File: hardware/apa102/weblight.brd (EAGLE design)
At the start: 31.8 x 12 mm, 16 parts, among them U1 ATtiny85-20SU

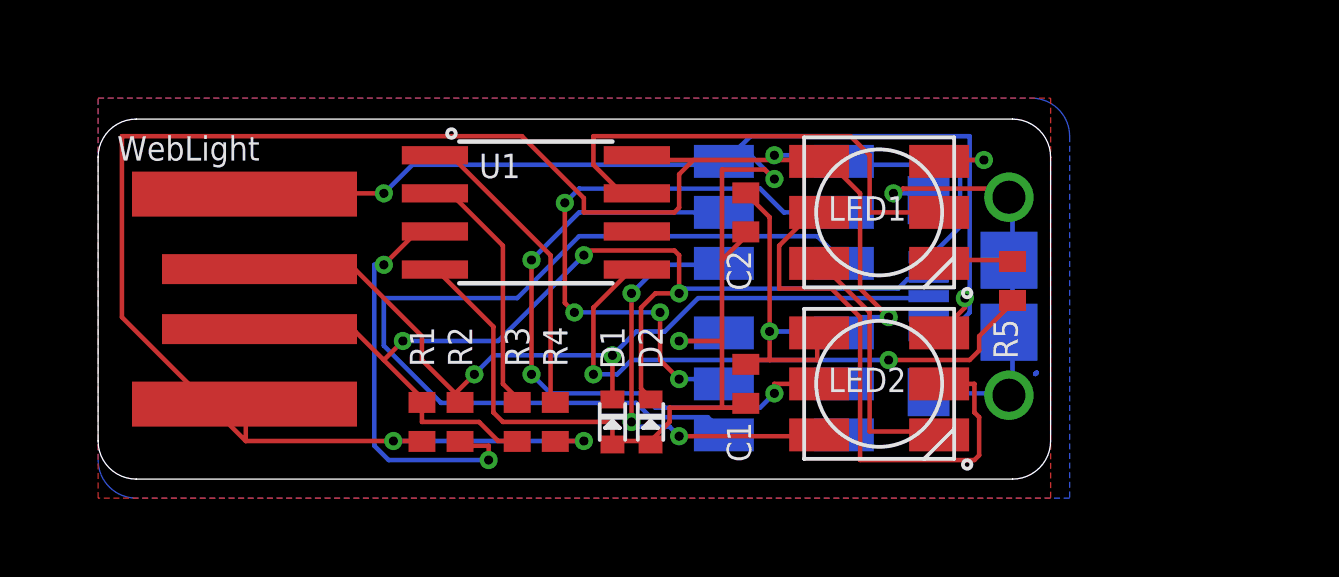
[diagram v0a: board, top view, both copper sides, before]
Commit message: Separate LED type and adopt new board versioning scheme
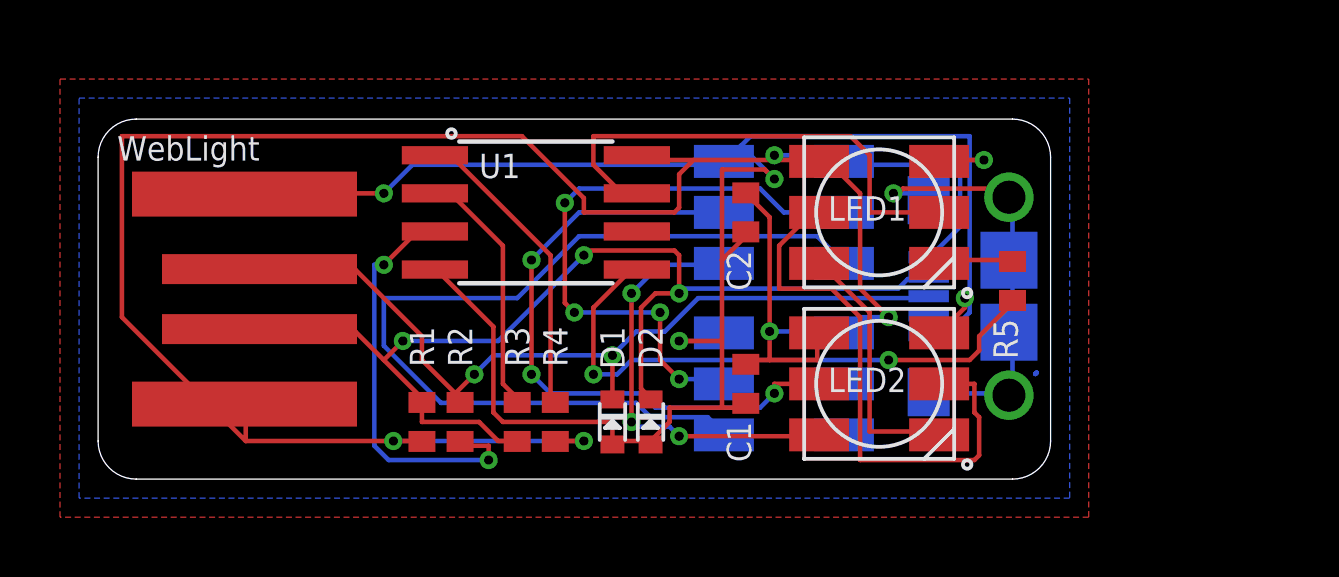
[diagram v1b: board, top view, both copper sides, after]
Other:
- board text added: "a-mf1"
- board text removed: "Version mf3"
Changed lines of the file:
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@@
 <wire x1="30.48" y1="12" x2="1.27" y2="12" width="0" layer="20"/>
 <wire x1="1.27" y1="12" x2="0" y2="10.73" width="0" layer="20" curve="90"/>
-<text x="1.27" y="0.635" size="1.016" layer="22" font="vector" rot="MR0" align="bottom-right">Version mf3</text>
+<text x="0.635" y="1.905" size="1.016" layer="22" font="vector" rot="MR0" align="bottom-right">a-mf1</text>
 <polygon width="0.4064" layer="43">
 <vertex x="0" y="12.065"/>
@@
 <vertex x="0" y="0"/>
 </polygon>
-<text x="1.27" y="2.54" size="0.8128" layer="22" font="vector" rot="MR0" align="bottom-right">sowbug.github.io/weblight</text>
+<text x="0.635" y="0.635" size="0.8128" layer="22" font="vector" rot="MR0" align="bottom-right">sowbug.github.io/weblight</text>
 <text x="0.635" y="11.43" size="0.8128" layer="21" font="vector" align="top-left">WebLight</text>
 </plain>
@@
 <via x="9.525" y="9.525" extent="1-16" drill="0.3048"/>
 <polygon width="0.4064" layer="1">
-<vertex x="0" y="12.7"/>
-<vertex x="31.75" y="12.7"/>
-<vertex x="31.75" y="-0.635"/>
-<vertex x="0" y="-0.635"/>
+<vertex x="-1.27" y="13.335"/>
+<vertex x="33.02" y="13.335"/>
+<vertex x="33.02" y="-1.27"/>
+<vertex x="-1.27" y="-1.27"/>
 </polygon>
 <polygon width="0.4064" layer="16">
-<vertex x="0" y="12.7"/>
-<vertex x="31.115" y="12.7" curve="-90"/>
-<vertex x="32.385" y="11.43"/>
+<vertex x="-0.635" y="12.7"/>
+<vertex x="32.385" y="12.7"/>
 <vertex x="32.385" y="-0.635"/>
-<vertex x="1.27" y="-0.635" curve="-90"/>
-<vertex x="0" y="0.635"/>
+<vertex x="-0.635" y="-0.635"/>
 </polygon>
 </signal>

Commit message: a-mf1
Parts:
- removed JP-USB-TOP: USBPCB, SparkFun-Connectors:USB-A-PCB
- removed R5: 470, rcl:R0402
- added HOLE1, HOLE2, HOLE3, HOLE4: MOUNTINGHOLE2.0, microbuilder:MOUNTINGHOLE_2.0_PLATED
- C1: value 10uF -> 1uF
- moved R1 16.2 mm to (26.7, 5.08), turned to 0 degrees
- moved LED4 16.1 mm to (8.13, 9.65), flipped to the top, turned to 180 degrees
- moved LED3 15.8 mm to (8.13, 3.05), flipped to the top, turned to 180 degrees
- moved R2 14.7 mm to (26.7, 3.81), turned to 180 degrees
- moved R3 12.7 mm to (26.7, 2.54), turned to 0 degrees
- moved D1 11.4 mm to (26.7, 8.26), turned to 90 degrees
- moved R4 11.4 mm to (26.7, 1.27), turned to 180 degrees
- moved LED1 11.3 mm to (14.7, 9.65), turned to 180 degrees
- moved LED2 11.3 mm to (14.7, 3.05), turned to 180 degrees
- moved D2 9.69 mm to (26.7, 6.99), turned to 90 degrees
- moved C1 9.69 mm to (26.7, 11.4), turned to 180 degrees
- moved U1 6.60 mm to (20.7, 6.35), turned to 0 degrees
- moved JP-USB-MICRO 6.36 mm to (35.3, 6.35), flipped to the top, turned to 90 degrees
- moved C2 5.24 mm to (26.7, 10.2), turned to 180 degrees
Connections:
- removed net DIN_RAW: R5.2, U1.5
- net DIN_1: now also U1.5; no longer R5.1
- net GND: now also C1.1, C2.1; no longer C1.2, C2.2, JP-USB-TOP.GND
- net USB_D_MINUS: now also R2.2; no longer R3.2
- net USB_D_MINUS_RAW: now also R1.2, R2.1; no longer JP-USB-TOP.USB_M, R1.1, R3.1
- net USB_D_PLUS: now also R3.1; no longer R2.2
- net USB_D_PLUS_RAW: now also R3.2; no longer JP-USB-TOP.USB_P, R2.1
- net VCC: now also C1.2, C2.2, R1.1; no longer C1.1, C2.1, JP-USB-TOP.5V, R1.2
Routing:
- net USB_D_MINUS_RAW: track 36.6 -> 10.6 mm, vias 3 -> 0
- net DIN_4: track 30.7 -> 8.36 mm
- net DIN_RAW: track 19.5 -> 0.00 mm, vias 2 -> 0
- net CLK_4: track 20.5 -> 8.51 mm, vias 4 -> 0
- net CLK_2: track 18.7 -> 8.60 mm
- net GND: track 68.8 -> 59.0 mm, vias 5 -> 4
- net VCC: track 84.2 -> 74.5 mm, vias 5 -> 4
- net DIN_1: track 2.56 -> 11.6 mm
- net CLK_3: track 21.4 -> 12.8 mm, vias 3 -> 0
- net USB_D_PLUS: track 14.1 -> 6.01 mm, vias 2 -> 0
- net CLK_1: track 16.5 -> 9.02 mm, vias 0 -> 2
- net USB_D_PLUS_RAW: track 28.0 -> 33.0 mm, vias 2 -> 0
- net SLD: track 15.2 -> 12.1 mm, vias 1 -> 0
- net DIN_3: track 14.2 -> 11.2 mm, vias 3 -> 2
- net N_RESET: track 10.2 -> 8.31 mm
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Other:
- board size 31.8 x 12 mm -> 38.1 x 12.7 mm
- board text removed: "sowbug.github.io/weblight"

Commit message: Forgot ICSP
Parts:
- added ICSP: POGOPIN-CONNONEHOLE, Protofusion:POGOPROG-CONN-1H
- JP-USB-MICRO: value (none) -> USB
- moved R4 5.08 mm to (21.6, 1.27)
- moved U1 1.27 mm to (20.7, 7.62)
- moved R2 1.27 mm to (26.7, 2.54), turned to 0 degrees
- moved R3 1.27 mm to (26.7, 1.27), turned to 180 degrees
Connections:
- removed net CLK_1: LED1.CI, U1.7
- removed net DIN_1: LED1.DI, U1.5
- new net CLK_1/SCK: ICSP.4, LED1.CI, U1.7
- new net DIN_1/MOSI: ICSP.2, LED1.DI, U1.5
- new net MISO: ICSP.3, U1.6
- net GND: now also ICSP.5
- net N_RESET: now also ICSP.1
- net USB_D_MINUS: now also R3.2; no longer R2.2
- net USB_D_MINUS_RAW: now also R3.1; no longer R2.1
- net USB_D_PLUS: now also R2.1; no longer R3.1
- net USB_D_PLUS_RAW: now also R2.2; no longer R3.2
- net VCC: now also ICSP.6
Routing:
- net DIN_1/MOSI: track 0.00 -> 27.4 mm, vias 0 -> 2
- net MISO: track 0.00 -> 16.8 mm, vias 0 -> 1
- net CLK_1/SCK: track 0.00 -> 15.9 mm, vias 0 -> 2
- net N_RESET: track 8.31 -> 20.3 mm, vias 0 -> 1
- net DIN_1: track 11.6 -> 0.00 mm
- net CLK_1: track 9.02 -> 0.00 mm, vias 2 -> 0
- net USB_D_MINUS_RAW: track 10.6 -> 13.8 mm
- net USB_D_PLUS_RAW: track 33.0 -> 30.1 mm, vias 0 -> 2
- net GND: track 59.0 -> 56.6 mm, vias 4 -> 3
- net VCC: track 74.5 -> 76.5 mm, vias 4 -> 3
- net DIN_3: track 11.2 -> 10.7 mm

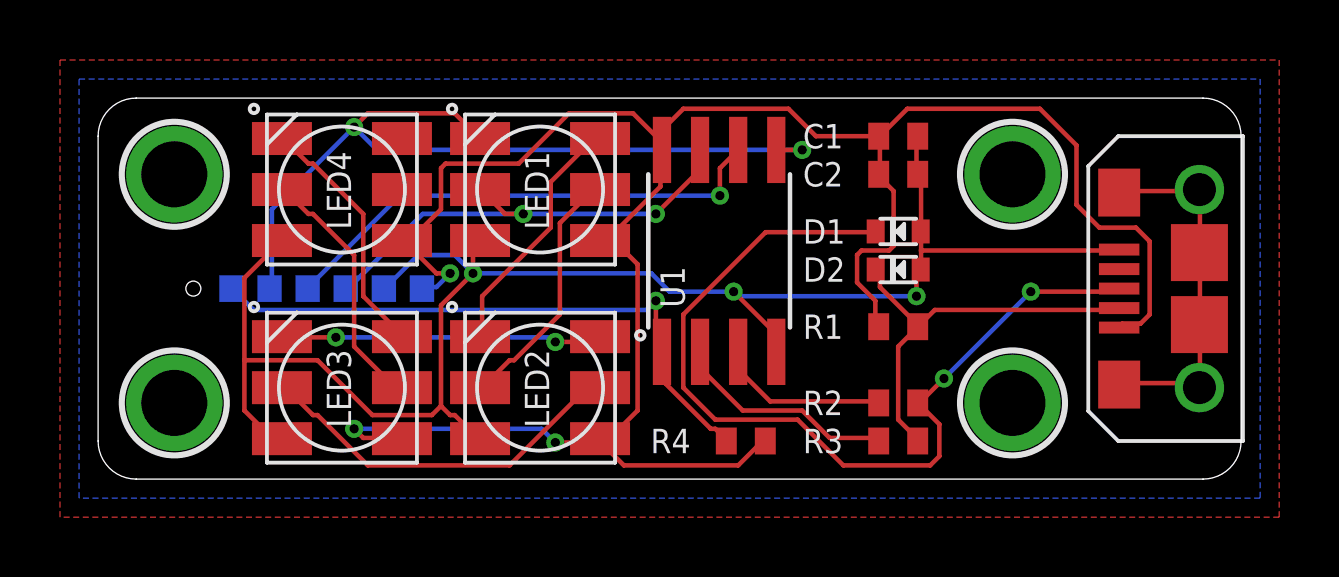
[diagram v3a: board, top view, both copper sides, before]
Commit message: Substitute 6-pin pogo layout
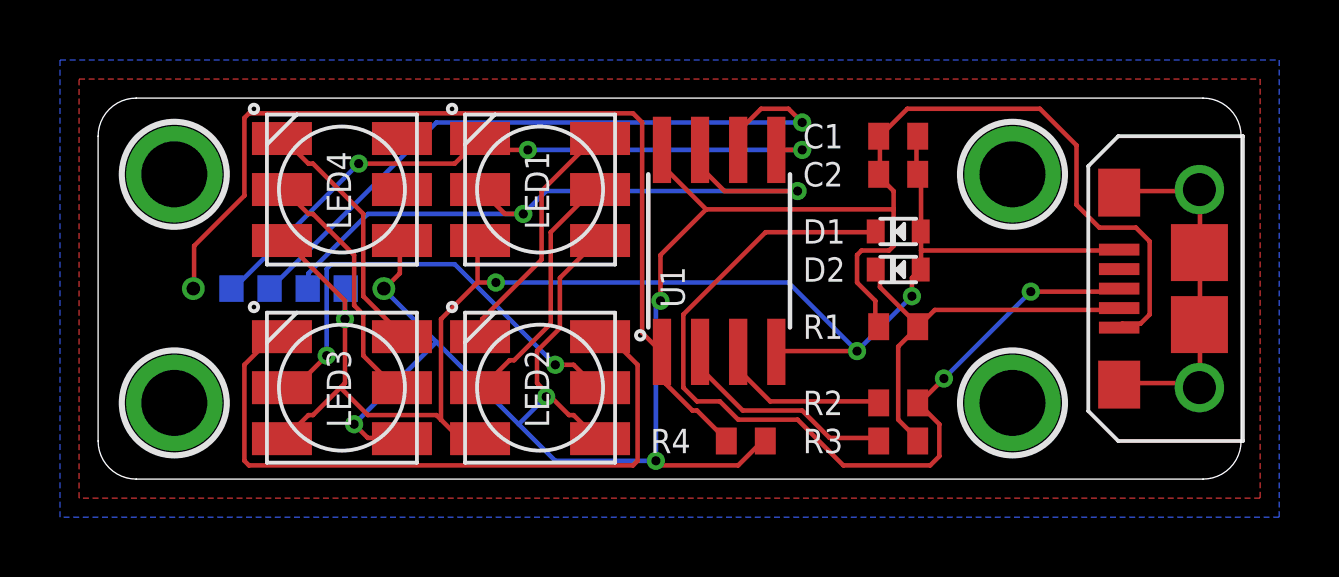
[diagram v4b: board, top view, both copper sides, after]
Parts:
- ICSP: value POGOPIN-CONNONEHOLE -> POGOPIN-CONNWITHVIAS; device Protofusion:POGOPROG-CONN-1H -> weblight:POGOPROG-CONN-0H
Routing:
- net DIN_3: track 10.7 -> 22.9 mm, vias 2 -> 0
- net N_RESET: track 20.3 -> 31.7 mm, vias 1 -> 0
- net CLK_1/SCK: track 15.9 -> 23.9 mm
- net MISO: track 16.8 -> 23.3 mm
- net DIN_1/MOSI: track 27.4 -> 22.1 mm, vias 2 -> 3
- net GND: track 56.6 -> 52.5 mm, vias 3 -> 4
- net CLK_3: track 12.8 -> 15.7 mm, vias 0 -> 2
- net VCC: track 76.5 -> 75.0 mm, vias 3 -> 4
